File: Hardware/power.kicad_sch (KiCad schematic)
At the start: 19 parts, among them IC2 AP2205-W5-7, J1 XT60PW-M, U4 TPSM863257RDXR

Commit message: Reorganised
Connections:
- net 5.5V renamed +5.5V
- net 5V renamed +5V
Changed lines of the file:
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@@
+	(wire
+		(pts
+			(xy 173.736 73.66) (xy 173.99 73.66)
+		)
+		(stroke
+			(width 0)
+			(type default)
+		)
+	)
 	(wire
 		(pts
@@
 	(wire
 		(pts
-			(xy 200.66 29.21) (xy 205.74 29.21)
+			(xy 200.66 29.21) (xy 207.518 29.21)
 		)
 		(stroke
@@
 	(wire
 		(pts
+			(xy 173.736 73.66) (xy 173.736 80.01)
+		)
+		(stroke
+			(width 0)
+			(type default)
+		)
+	)
+	(wire
+		(pts
 			(xy 158.75 68.58) (xy 162.56 68.58)
 		)
@@
 		(pts
 			(xy 176.53 33.02) (xy 166.37 33.02)
-		)
-		(stroke
-			(width 0)
-			(type default)
-		)
-	)
-	(wire
-		(pts
-			(xy 173.736 76.708) (xy 173.736 80.01)
 		)
 		(stroke
@@
 			)
 			(justify left bottom)
-		)
-	)
-	(hierarchical_label "5.5V"
-		(shape output)
-		(at 205.74 29.21 0)
-		(effects
-			(font
-				(size 1.27 1.27)
-			)
-			(justify left)
-		)
-	)
-	(hierarchical_label "5V"
-		(shape output)
-		(at 173.736 76.708 90)
-		(effects
-			(font
-				(size 1.27 1.27)
-			)
-			(justify left)
 		)
 	)
@@
 	)
 	(symbol
+		(lib_id "power:+5V")
+		(at 207.518 29.21 0)
+		(unit 1)
+		(exclude_from_sim no)
+		(in_bom yes)
+		(on_board yes)
+		(dnp no)
+		(fields_autoplaced yes)
+		(property "Reference" "#PWR033"
+			(at 207.518 33.02 0)
+			(effects
+				(font
+					(size 1.27 1.27)
+				)
+				(hide yes)
+			)
+		)
+		(property "Value" "+5.5V"
+			(at 207.518 24.13 0)
+			(effects
+				(font
+					(size 1.27 1.27)
+				)
+			)
+		)
+		(property "Footprint" ""
+			(at 207.518 29.21 0)
+			(effects
+				(font
+					(size 1.27 1.27)
+				)
+				(hide yes)
+			)
+		)
+		(property "Datasheet" ""
+			(at 207.518 29.21 0)
+			(effects
+				(font
+					(size 1.27 1.27)
+				)
+				(hide yes)
+			)
+		)
+		(property "Description" "Power symbol creates a global label with name \"+5V\""
+			(at 207.518 29.21 0)
+			(effects
+				(font
+					(size 1.27 1.27)
+				)
+				(hide yes)
+			)
+		)
+		(pin "1"
+		)
+		(instances
+			(project "Pi-based PCB"
+				(path "/e4035b22-64c9-4a42-9837-ade8aec3882f/3ae90f15-a57a-41c5-834b-f728dd5efad8"
+					(reference "#PWR033")
+					(unit 1)
+				)
+			)
+		)
+	)
+	(symbol
 		(lib_id "power:GND")
 		(at 189.23 66.04 0)
@@
 		)
 		(instances
-			(project ""
+			(project "Pi-based PCB"
 				(path "/e4035b22-64c9-4a42-9837-ade8aec3882f/3ae90f15-a57a-41c5-834b-f728dd5efad8"
 					(reference "U4")
@@
 		)
 		(instances
-			(project ""
+			(project "Pi-based PCB"
 				(path "/e4035b22-64c9-4a42-9837-ade8aec3882f/3ae90f15-a57a-41c5-834b-f728dd5efad8"
 					(reference "#PWR016")
+					(unit 1)
+				)
+			)
+		)
+	)
+	(symbol
+		(lib_id "power:+5V")
+		(at 173.99 73.66 0)
+		(unit 1)
+		(exclude_from_sim no)
+		(in_bom yes)
+		(on_board yes)
+		(dnp no)
+		(fields_autoplaced yes)
+		(property "Reference" "#PWR031"
+			(at 173.99 77.47 0)
+			(effects
+				(font
+					(size 1.27 1.27)
+				)
+				(hide yes)
+			)
+		)
+		(property "Value" "+5V"
+			(at 173.99 68.58 0)
+			(effects
+				(font
+					(size 1.27 1.27)
+				)
+			)
+		)
+		(property "Footprint" ""
+			(at 173.99 73.66 0)
+			(effects
+				(font
+					(size 1.27 1.27)
+				)
+				(hide yes)
+			)
+		)
+		(property "Datasheet" ""
+			(at 173.99 73.66 0)
+			(effects
+				(font
+					(size 1.27 1.27)
+				)
+				(hide yes)
+			)
+		)
+		(property "Description" "Power symbol creates a global label with name \"+5V\""
+			(at 173.99 73.66 0)
+			(effects
+				(font
+					(size 1.27 1.27)
+				)
+				(hide yes)
+			)
+		)
+		(pin "1"
+		)
+		(instances
+			(project "Pi-based PCB"
+				(path "/e4035b22-64c9-4a42-9837-ade8aec3882f/3ae90f15-a57a-41c5-834b-f728dd5efad8"
+					(reference "#PWR031")
 					(unit 1)
 				)
@@
 		)
 		(instances
-			(project ""
+			(project "Pi-based PCB"
 				(path "/e4035b22-64c9-4a42-9837-ade8aec3882f/3ae90f15-a57a-41c5-834b-f728dd5efad8"
 					(reference "J1")

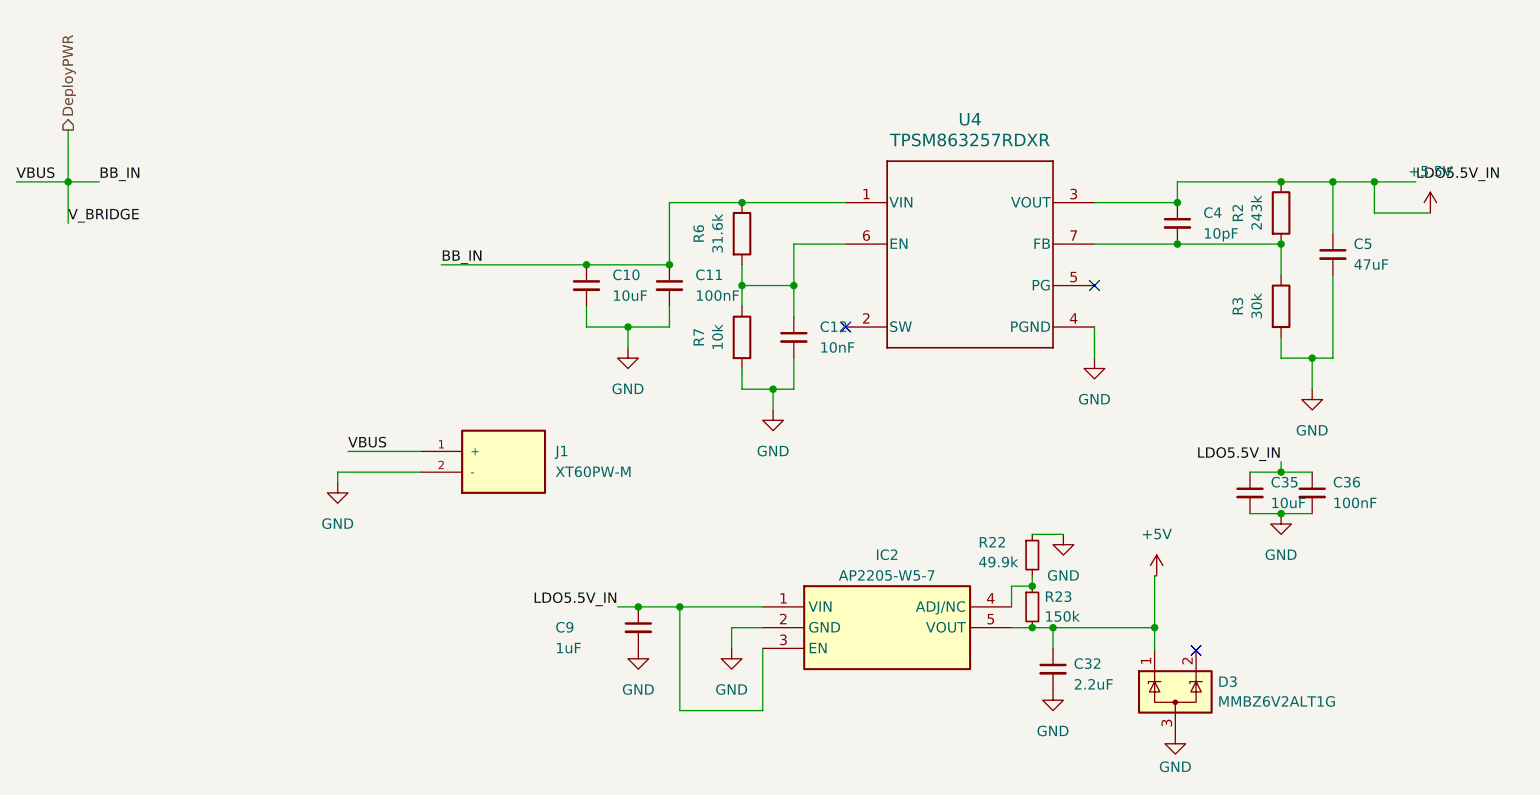
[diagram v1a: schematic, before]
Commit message: Modified power
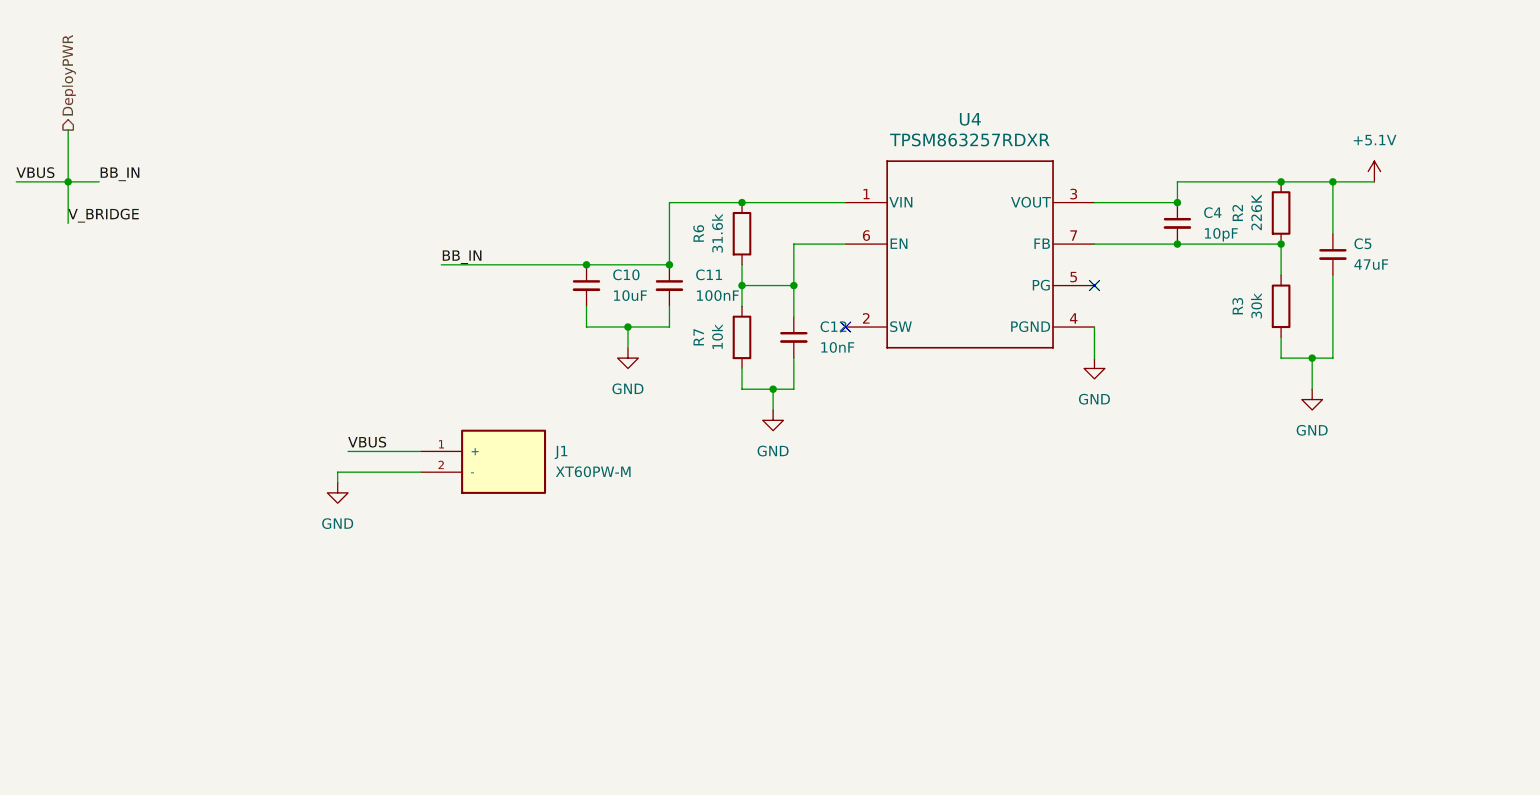
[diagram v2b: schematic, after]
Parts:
- removed C32: 2.2uF, Capacitor_SMD:C_0402_1005Metric, symbol Device:C_Small
- removed C35: 10uF, Capacitor_SMD:C_0402_1005Metric, symbol Device:C_Small
- removed C36: 100nF, Capacitor_SMD:C_0402_1005Metric, symbol Device:C_Small
- removed C9: 1uF, Capacitor_SMD:C_0402_1005Metric, symbol Device:C_Small
- removed D3: MMBZ6V2ALT1G, Package_TO_SOT_SMD:SOT-23, symbol Power_Protection:SP0502BAHT
- removed IC2: AP2205-W5-7, iclr:SOT95P282X145-5N, symbol iclr:AP2205-W5-7
- removed R22: 49.9k, Resistor_SMD:R_0402_1005Metric, symbol Device:R_Small
- removed R23: 150k, Resistor_SMD:R_0402_1005Metric, symbol Device:R_Small
- R2: value 243k -> 226K
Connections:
- net +5.5V renamed +5.1V
- no-connect marks 3 -> 2
